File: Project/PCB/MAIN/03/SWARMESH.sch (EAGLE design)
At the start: 49 parts, among them IC1 L7805CV-DG, Q1 TIP122, U1 ESP32DEVKITC, U2 TCRT5000L, U3 L293D, U5 TCRT5000L, U6 CD4051BEE4

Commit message: started v3 of PCB
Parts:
- removed R13: 1k, adafruit:R-US_0207/9
- removed RD1, RD2: 0, adafruit:R-US_0207/9
- removed RS1: 220, adafruit:R-US_0207/9
- added R1: 220, adafruit:R-US_0207/9
- added RB: 1k, adafruit:R-US_0207/9
- added RD: 0, adafruit:R-US_0207/9
- C2: device adafruit:C-USC0805 -> adafruit:C-US025-030X050
- U2: value TCRT5000L -> CD4051BEE4; device TCRT5000L:TCRT5000L -> CD4051BEE4:CD4051BEE4
- U6: value CD4051BEE4 -> TCRT5000L; device CD4051BEE4:CD4051BEE4 -> TCRT5000L:TCRT5000L
- renumbered IC1 to U4
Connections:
- removed net N$1: Q1.C, RD1.1
- net ADCMX: now also U2.COM_OUT/IN; no longer U6.COM_OUT/IN
- net GND: now also RD.2, U6.C, U6.E; no longer RD2.2, U2.C, U2.E
- net IO5: now also U2.A; no longer U6.A
- net IR2: now also U6.CO; no longer U2.CO
- net IRTX: now also RB.2; no longer R13.2
- net N$11: now also U2.CHANNELS_IN/OUT_4; no longer U6.CHANNELS_IN/OUT_4
- net N$12: now also RB.1, U2.INH, U2.VEE, U2.VSS; no longer R13.1, U6.INH, U6.VEE, U6.VSS
- net N$13: now also U2.CHANNELS_IN/OUT_6; no longer U6.CHANNELS_IN/OUT_6
- net N$14: now also U2.CHANNELS_IN/OUT_7; no longer U6.CHANNELS_IN/OUT_7
- net N$16: now also R1.1; no longer RS1.1
- net N$17: now also Q1.C, RD.1; no longer RD1.2, RD2.1
- net N$19: now also U2.CHANNELS_IN/OUT_0; no longer U6.CHANNELS_IN/OUT_0
- net N$20: now also U2.CHANNELS_IN/OUT_1; no longer U6.CHANNELS_IN/OUT_1
- net N$21: now also U2.CHANNELS_IN/OUT_3; no longer U6.CHANNELS_IN/OUT_3
- net N$22: now also U2.CHANNELS_IN/OUT_2; no longer U6.CHANNELS_IN/OUT_2
- net N$5: now also U2.CHANNELS_IN/OUT_5; no longer U6.CHANNELS_IN/OUT_5
- net N$7: now also U2.B; no longer U6.B
- net N$8: now also U2.C; no longer U6.C
- net N$9: now also U6.A; no longer U2.A
- net VCC: now also R1.2, U2.VDD; no longer RS1.2, U6.VDD
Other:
- note added: "Note: Solder RB and Q1 or RD to configure IR operation"
- note removed: "Note: Select RS & RD to configure IR operation"
- note removed: "Note: We are using 5V + 22ohm resistor to control the Emitter"
- moved on the sheet: Q1

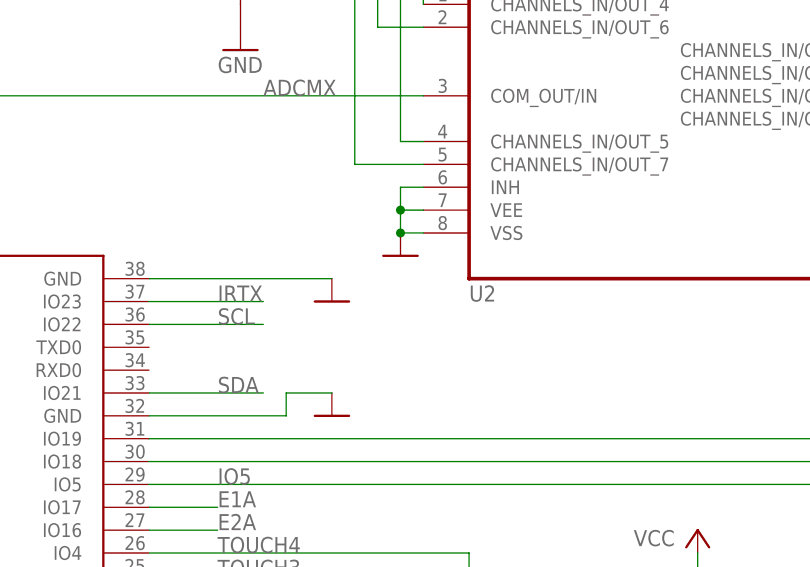
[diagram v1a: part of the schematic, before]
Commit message: added power net to PCB, corrected orphan GND network in SCH
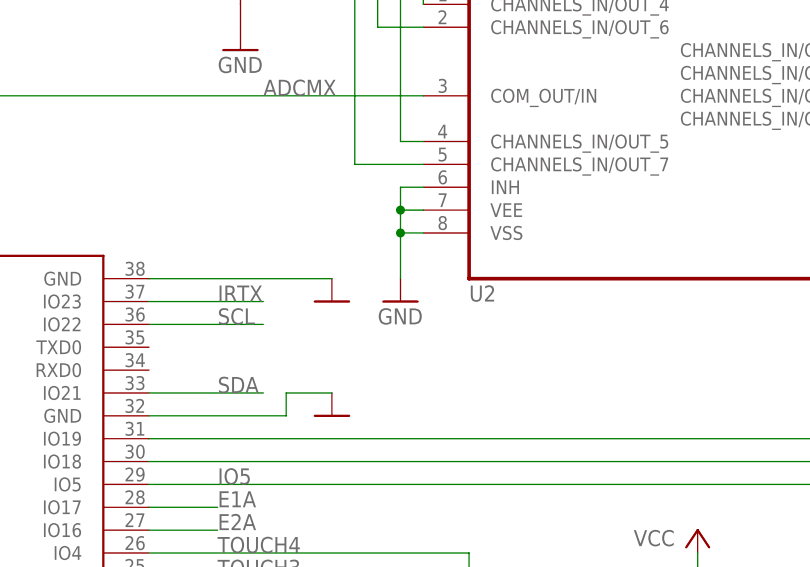
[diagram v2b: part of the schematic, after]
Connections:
- removed net N$12: Q1.B, RB.1, U2.INH, U2.VEE, U2.VSS
- new net N$1: Q1.B, RB.1
- net GND: now also U2.INH, U2.VEE, U2.VSS
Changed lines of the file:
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@@
 <part name="F1" library="RUEF300K-2" deviceset="RUEF300K-2" device="" value="RUEF300K-2"/>
 <part name="JMUX" library="adafruit" deviceset="PINHD-1X10" device=""/>
-<part name="GND9" library="supply1" deviceset="GND" device=""/>
 <part name="U2" library="CD4051BEE4" deviceset="CD4051BEE4" device=""/>
 <part name="P+6" library="supply1" library_urn="urn:adsk.eagle:library:371" deviceset="VCC" device=""/>
@@
 <part name="C2" library="adafruit" library_urn="urn:adsk.eagle:library:420" deviceset="C-US" device="025-030X050" package3d_urn="urn:adsk.eagle:package:6240322/1"/>
 <part name="R1" library="adafruit" library_urn="urn:adsk.eagle:library:420" deviceset="R-US_" device="0207/9" package3d_urn="urn:adsk.eagle:package:6240935/1" value="220"/>
+<part name="GND14" library="supply1" deviceset="GND" device=""/>
 </parts>
 <sheets>
@@
 <attribute name="VALUE" x="349.25" y="132.08" size="1.778" layer="96" display="off"/>
 </instance>
-<instance part="GND9" gate="1" x="264.16" y="132.08">
-<attribute name="VALUE" x="261.62" y="129.54" size="1.778" layer="96" display="off"/>
-</instance>
 <instance part="U2" gate="G$1" x="299.72" y="144.78">
 <attribute name="NAME" x="271.78" y="127" size="1.778" layer="95"/>
@@
 <attribute name="NAME" x="313.69" y="97.5614" size="1.778" layer="95" rot="R180"/>
 <attribute name="VALUE" x="314.452" y="92.456" size="1.778" layer="96" rot="R180"/>
+</instance>
+<instance part="GND14" gate="1" x="264.16" y="127">
+<attribute name="VALUE" x="261.62" y="124.46" size="1.778" layer="96"/>
 </instance>
 </instances>
@@
 <pinref part="GND20" gate="1" pin="GND"/>
 <wire x1="142.24" y1="144.78" x2="142.24" y2="143.51" width="0.1524" layer="91"/>
+</segment>
+<segment>
+<pinref part="U2" gate="G$1" pin="INH"/>
+<wire x1="266.7" y1="139.7" x2="264.16" y2="139.7" width="0.1524" layer="91"/>
+<wire x1="264.16" y1="139.7" x2="264.16" y2="137.16" width="0.1524" layer="91"/>
+<pinref part="GND14" gate="1" pin="GND"/>
+<pinref part="U2" gate="G$1" pin="VSS"/>
+<wire x1="264.16" y1="137.16" x2="264.16" y2="134.62" width="0.1524" layer="91"/>
+<wire x1="264.16" y1="134.62" x2="264.16" y2="129.54" width="0.1524" layer="91"/>
+<wire x1="266.7" y1="134.62" x2="264.16" y2="134.62" width="0.1524" layer="91"/>
+<pinref part="U2" gate="G$1" pin="VEE"/>
+<wire x1="266.7" y1="137.16" x2="264.16" y2="137.16" width="0.1524" layer="91"/>
+<junction x="264.16" y="137.16"/>
+<junction x="264.16" y="134.62"/>
 </segment>
 </net>
@@
 </segment>
 </net>
-<net name="N$12" class="0">
-<segment>
-<pinref part="RB" gate="G$1" pin="1"/>
-<pinref part="Q1" gate="G$1" pin="B"/>
-<wire x1="317.5" y1="81.28" x2="322.58" y2="81.28" width="0.1524" layer="91"/>
-</segment>
-<segment>
-<pinref part="U2" gate="G$1" pin="VSS"/>
-<pinref part="U2" gate="G$1" pin="VEE"/>
-<wire x1="266.7" y1="137.16" x2="264.16" y2="137.16" width="0.1524" layer="91"/>
-<wire x1="264.16" y1="137.16" x2="264.16" y2="134.62" width="0.1524" layer="91"/>
-<wire x1="266.7" y1="134.62" x2="264.16" y2="134.62" width="0.1524" layer="91"/>
-<junction x="264.16" y="134.62"/>
-<pinref part="GND9" gate="1" pin="GND"/>
-<pinref part="U2" gate="G$1" pin="INH"/>
-<wire x1="266.7" y1="139.7" x2="264.16" y2="139.7" width="0.1524" layer="91"/>
-<wire x1="264.16" y1="139.7" x2="264.16" y2="137.16" width="0.1524" layer="91"/>
-<junction x="264.16" y="137.16"/>
-</segment>
-</net>
 <net name="N$15" class="0">
 <segment>
@@
 </segment>
 </net>
+<net name="N$1" class="0">
+<segment>
+<pinref part="RB" gate="G$1" pin="1"/>
+<pinref part="Q1" gate="G$1" pin="B"/>
+<wire x1="317.5" y1="81.28" x2="322.58" y2="81.28" width="0.1524" layer="91"/>
+</segment>
+</net>
